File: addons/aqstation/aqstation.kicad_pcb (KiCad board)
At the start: 2 copper layers, 76 x 50 mm, 15 parts, among them J1 PMSA003, J2 Conn_02x06_Odd_Even, J3 Adafruit_I2C_Header, J5 RGB_Header, J6 Pimoroni_I2CGarden_Header, J7 StemmaQT_Qwiic_Header, J8 BME680_Header

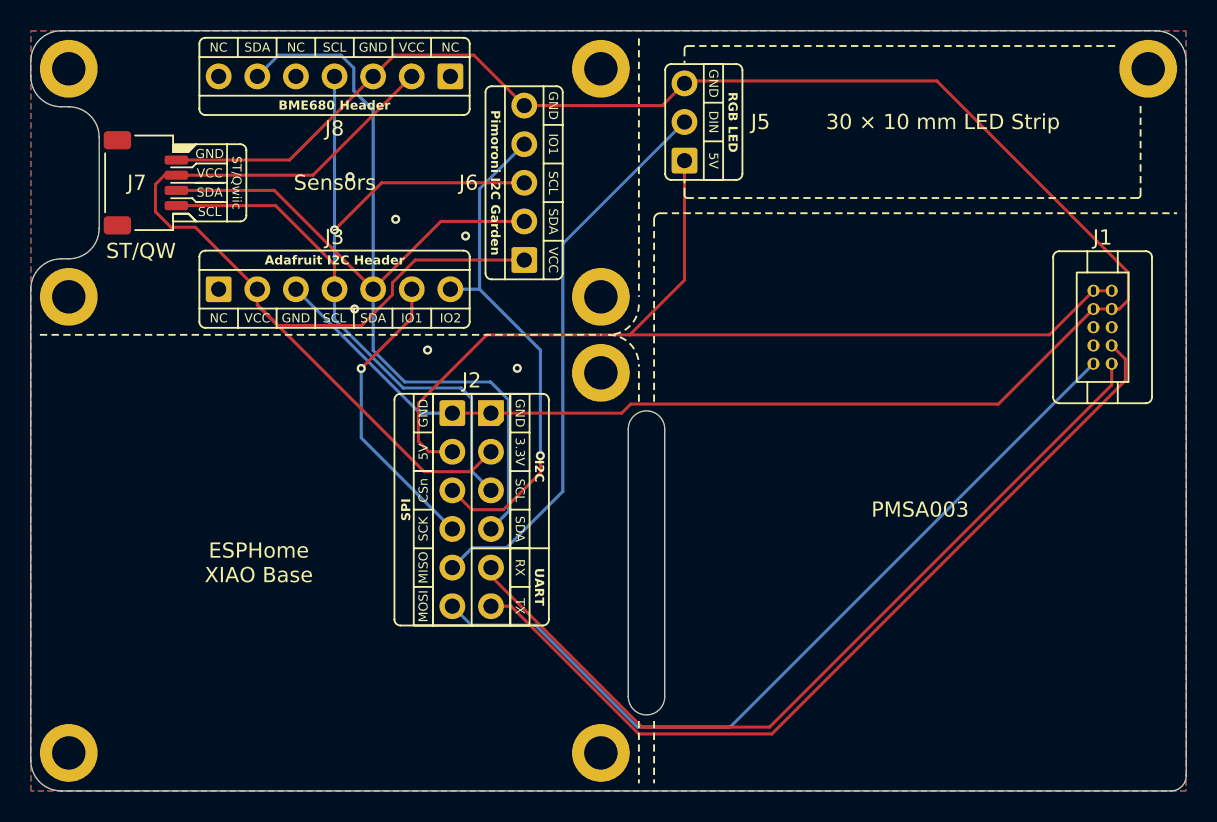
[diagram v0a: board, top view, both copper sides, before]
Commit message: More compact version of the AQStation
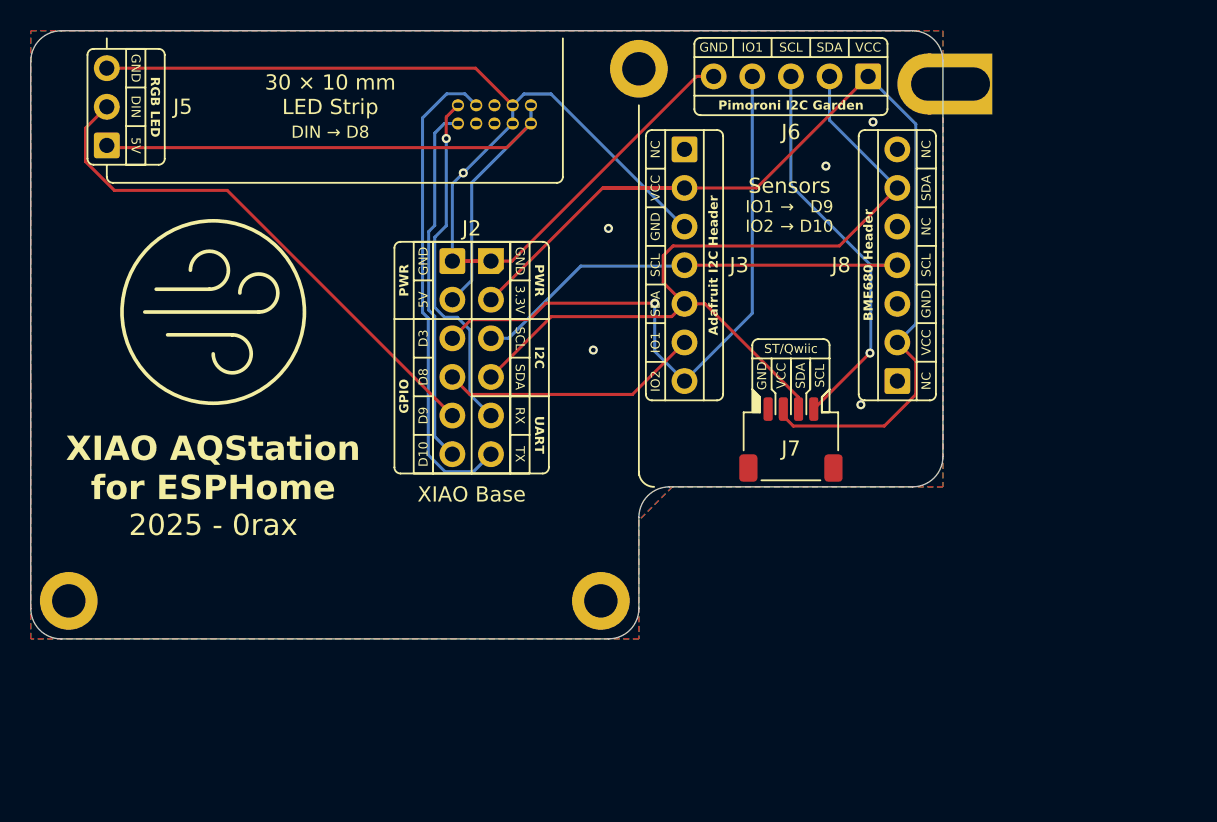
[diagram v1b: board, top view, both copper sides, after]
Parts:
- removed H1, H5, H6, H8: MountingHole_2.2mm_M2_ISO14580_Pad, MountingHole:MountingHole_2.2mm_M2_ISO14580_Pad
- H2: value MountingHole_2.2mm_M2_ISO14580_Pad -> MountingHole_M2_Slot; footprint MountingHole:MountingHole_2.2mm_M2_ISO14580_Pad -> LKBD_MountingHole:MountingHole_M2_Slot
- J1: moved to B.Cu
- moved H3 79.2 mm to (32.5, 67.5)
- moved H7 58.6 mm to (70.0, 32.5)
- moved J7 45.7 mm to (80.0, 56.9), turned to 0 degrees
- moved H4 40.3 mm to (67.5, 67.5)
- moved J1 39.8 mm to (68.0, 30.0), turned to 180 degrees
- moved J8 39.0 mm to (87.0, 45.4), turned to 180 degrees
- moved J5 38.0 mm to (35.0, 35.0)
- moved H2 24.5 mm to (92.0, 33.5), turned to 180 degrees
- moved J3 23.1 mm to (73.0, 45.4), turned to 0 degrees
- moved J6 18.9 mm to (80.0, 33.0), turned to -90 degrees
- moved J2 10.0 mm to (59.0, 51.5)
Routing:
- net GND: track 135.8 -> 79.6 mm
- net /RX: track 56.2 -> 23.1 mm, vias 0 -> 1
- net /D3: track 55.4 -> 23.7 mm
- net /TX: track 57.5 -> 31.9 mm
- net +5V: track 66.6 -> 43.6 mm
- net /SDA: track 73.7 -> 55.7 mm
- net /D10: track 33.7 -> 42.1 mm
- net /SCL: track 61.2 -> 56.1 mm
- net +3.3V: track 74.6 -> 71.7 mm
- net /D9: track 19.8 -> 17.2 mm, vias 1 -> 0
- net /D8: track 37.0 -> 35.2 mm
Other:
- board size 76 x 50 mm -> 60 x 40 mm
- board text added: "0.1600 mm / 0.1600 mm"
- board text added: "0.3000 mm"
- board text added: "1.6000 mm"
- board text added: "2"
- board text added: "60.0000 mm x 40.0000 mm"
- board text added: "BOARD CHARACTERISTICS"
- board text added: "Board Thickness:"
- board text added: "Board overall dimensions:"
- board text added: "Castellated pads:"
- board text added: "Copper Finish:"
- board text added: "Copper Layer Count:"
- board text added: "D9 D10"
- board text added: "DIN → D8"
- board text added: "Edge card connectors:"
- board text added: "HAL lead-free"
- board text added: "IO1 IO2"
- board text added: "Impedance Control:"
- board text added: "Min hole diameter:"
- board text added: "Min track/spacing:"
- board text added: "No"
- board text added: "Plated Board Edge:"
- board text added: "XIAO Base"
- board text added: "→ →"
- board text removed: "ESPHome XIAO Base"
- board text removed: "ST/QW"

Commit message: Switch LED header to just some pads
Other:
- board text added: "SET → D3"

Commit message: Remove solderpaste from pcbdraw export
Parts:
- added H5: MountingHole_2.2mm_M2_ISO14580_Pad, MountingHole:MountingHole_2.2mm_M2_ISO14580_Pad, F.Cu at (87.5, 57.5)
- renumbered H7 to H1
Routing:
- net +3.3V: track 71.7 -> 68.5 mm
- net GND: vias 6 -> 4

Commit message: Cleanup wiring
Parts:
- added H5: MountingHole_2.2mm_M2_ISO14580_Pad, MountingHole:MountingHole_2.2mm_M2_ISO14580_Pad, F.Cu at (67.5, 42.5)
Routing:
- net +3.3V: track 68.5 -> 62.0 mm
- net /D10: track 42.1 -> 39.4 mm
- net GND: track 79.6 -> 77.1 mm, vias 4 -> 3
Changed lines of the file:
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@@
 		)
 	)
+	(footprint "MountingHole:MountingHole_2.2mm_M2_ISO14580_Pad"
+		(layer "F.Cu")
+		(at 67.5 42.5)
+		(descr "Mounting Hole 2.2mm, M2, ISO14580")
+		(tags "mounting hole 2.2mm m2 iso14580")
+		(property "Reference" "H5"
+			(at 0 -2.9 0)
+			(layer "F.SilkS")
+			(hide yes)
+			(effects
+				(font
+					(size 1 1)
+					(thickness 0.15)
+				)
+			)
+		)
+		(property "Value" "MountingHole_2.2mm_M2_ISO14580_Pad"
+			(at 0 2.9 0)
+			(layer "F.Fab")
+			(effects
+				(font
+					(size 1 1)
+					(thickness 0.15)
+				)
+			)
+		)
+		(property "Datasheet" ""
+			(at 0 0 0)
+			(unlocked yes)
+			(layer "F.Fab")
+			(hide yes)
+			(effects
+				(font
+					(size 1.27 1.27)
+					(thickness 0.15)
+				)
+			)
+		)
+		(property "Description" ""
+			(at 0 0 0)
+			(unlocked yes)
+			(layer "F.Fab")
+			(hide yes)
+			(effects
+				(font
+					(size 1.27 1.27)
+					(thickness 0.15)
+				)
+			)
+		)
+		(attr board_only exclude_from_pos_files exclude_from_bom)
+		(fp_circle
+			(center 0 0)
+			(end 1.9 0)
+			(stroke
+				(width 0.15)
+				(type solid)
+			)
+			(fill no)
+			(layer "Cmts.User")
+		)
+		(fp_circle
+			(center 0 0)
+			(end 2.15 0)
+			(stroke
+				(width 0.05)
+				(type solid)
+			)
+			(fill no)
+			(layer "F.CrtYd")
+		)
+		(fp_text user "${REFERENCE}"
+			(at 0 0 0)
+			(layer "F.Fab")
+			(effects
+				(font
+					(size 1 1)
+					(thickness 0.15)
+				)
+			)
+		)
+		(pad "1" thru_hole circle
+			(at 0 0)
+			(size 3.8 3.8)
+			(drill 2.2)
+			(layers "*.Cu" "*.Mask")
+			(remove_unused_layers no)
+		)
+		(embedded_fonts no)
+	)
 	(footprint "LKBD_MountingHole:MountingHole_M2_Slot"
 		(layer "F.Cu")
@@
 	)
 	(segment
-		(start 35 32.46)
-		(end 59.26 32.46)
+		(start 60.27 45.15)
+		(end 69.52 35.9)
 		(width 0.2)
 		(layer "F.Cu")
@@
 	)
 	(segment
-		(start 57.73 45.15)
-		(end 60.27 45.15)
+		(start 35 32.46)
+		(end 59.26 32.46)
 		(width 0.2)
 		(layer "F.Cu")
@@
 	(segment
 		(start 57.73 45.15)
-		(end 61.65 45.15)
+		(end 60.27 45.15)
 		(width 0.2)
 		(layer "F.Cu")
@@
 	)
 	(segment
-		(start 61.65 45.15)
-		(end 73.8 33)
+		(start 69.52 35.9)
+		(end 72.02 35.9)
 		(width 0.2)
 		(layer "F.Cu")
@@
 	)
 	(segment
-		(start 73.8 33)
-		(end 74.92 33)
+		(start 74.92 33)
+		(end 72.02 35.9)
 		(width 0.2)
 		(layer "F.Cu")
@@
 	)
 	(via
-		(at 68 43)
+		(at 68.9 47.3)
 		(size 0.6)
 		(drill 0.3)
 		(layers "F.Cu" "B.Cu")
+		(free yes)
 		(net 1)
 	)
@@
 	)
 	(via
-		(at 67 51)
-		(size 0.6)
-		(drill 0.3)
-		(layers "F.Cu" "B.Cu")
-		(net 1)
-	)
-	(via
 		(at 82.3 38.9)
 		(size 0.6)
@@
 	)
 	(segment
-		(start 73 40.34)
-		(end 71.64 40.34)
+		(start 60.56 47.4)
+		(end 60.27 47.69)
 		(width 0.2)
 		(layer "F.Cu")
@@
 	)
 	(segment
-		(start 79.5 55.659999)
-		(end 79.940001 56.1)
+		(start 77.74 40.34)
+		(end 85.08 33)
 		(width 0.2)
 		(layer "F.Cu")
@@
 	)
 	(segment
-		(start 87 51.009196)
-		(end 87 50.5)
+		(start 73 40.34)
+		(end 73 40.7)
 		(width 0.2)
 		(layer "F.Cu")
@@
 	)
 	(segment
-		(start 67.62 40.34)
-		(end 77.74 40.34)
+		(start 66.3 47.4)
+		(end 60.56 47.4)
+		(width 0.2)
+		(layer "F.Cu")
+		(net 2)
+	)
+	(segment
+		(start 79.5 55.659999)
+		(end 79.940001 56.1)
 		(width 0.2)
 		(layer "F.Cu")
@@
 	)
 	(segment
-		(start 67.62 40.34)
-		(end 73 40.34)
+		(start 87 51.009196)
+		(end 87 50.5)
 		(width 0.2)
 		(layer "F.Cu")
@@
 	)
 	(segment
-		(start 60.27 47.69)
-		(end 67.62 40.34)
+		(start 73 40.7)
+		(end 66.3 47.4)
 		(width 0.2)
 		(layer "F.Cu")
@@
 	)
 	(segment
-		(start 77.74 40.34)
-		(end 85.08 33)
+		(start 73 40.34)
+		(end 77.74 40.34)
 		(width 0.2)
 		(layer "F.Cu")
@@
 	)
 	(segment
-		(start 87 40.34)
-		(end 83.19 44.15)
+		(start 63.14 49.9)
+		(end 60.27 52.77)
 		(width 0.2)
 		(layer "F.Cu")
@@
 	)
 	(segment
-		(start 72.16 48.8)
-		(end 64.24 48.8)
+		(start 87 40.34)
+		(end 83.19 44.15)
 		(width 0.2)
 		(layer "F.Cu")
@@
 	)
 	(segment
-		(start 64.24 48.8)
-		(end 60.27 52.77)
-		(width 0.2)
-		(layer "F.Cu")
-		(net 4)
-	)
-	(segment
 		(start 83.19 44.15)
 		(end 72.25 44.15)
@@
 	(segment
 		(start 73 47.96)
-		(end 72.16 48.8)
+		(end 71.06 49.9)
 		(width 0.2)
 		(layer "F.Cu")
@@
 	)
 	(segment
+		(start 71.06 49.9)
+		(end 63.14 49.9)
+		(width 0.2)
+		(layer "F.Cu")
+		(net 4)
+	)
+	(segment
 		(start 71.6 46.56)
 		(end 73 47.96)
@@
 	)
 	(segment
-		(start 69.579 53.921)
-		(end 73 50.5)
+		(start 58.96 54)
+		(end 61.2 54)
 		(width 0.2)
 		(layer "F.Cu")
@@
 	)
 	(segment
-		(start 58.881 53.921)
-		(end 69.579 53.921)
+		(start 61.2 54)
+		(end 64.7 50.5)
 		(width 0.2)
 		(layer "F.Cu")
@@
 	)
 	(segment
-		(start 57.73 52.77)
-		(end 58.881 53.921)
+		(start 64.7 50.5)
+		(end 73 50.5)
 		(width 0.2)
 		(layer "F.Cu")
@@
 	)
 	(segment
-		(start 58.96 49)
-		(end 62.8 49)
-		(width 0.2)
-		(layer "F.Cu")
-		(net 18)
-	)
-	(segment
-		(start 62.8 49)
-		(end 63.8818 47.9182)
+		(start 57.73 52.77)
+		(end 58.96 54)
 		(width 0.2)
 		(layer "F.Cu")
-		(net 18)
+		(net 17)
 	)
 	(segment
-		(start 57.73 50.23)
+		(start 69.1 49)
 		(end 58.96 49)
 		(width 0.2)
@@
 	)
 	(segment
-		(start 63.8818 47.9182)
-		(end 71.0427 47.9182)
+		(start 58.96 49)
+		(end 57.73 50.23)
 		(width 0.2)
 		(layer "F.Cu")
@@
 	)
 	(via
-		(at 71.0427 47.9182)
+		(at 69.1 49)
 		(size 0.6)
 		(drill 0.3)
@@
 	)
 	(segment
+		(start 73 52.9182)
+		(end 73 53.04)
+		(width 0.2)
+		(layer "B.Cu")
+		(net 18)
+	)
+	(segment
 		(start 77.46 48.58)
 		(end 73 53.04)
@@
 	)
 	(segment
-		(start 71.0427 51.0827)
-		(end 71.0427 47.9182)
+		(start 69.1 49)
+		(end 69.1 49.0182)
 		(width 0.2)
 		(layer "B.Cu")
@@
 	)
 	(segment
-		(start 73 53.04)
-		(end 71.0427 51.0827)
+		(start 69.1 49.0182)
+		(end 73 52.9182)
 		(width 0.2)
 		(layer "B.Cu")

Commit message: Finalize aqstation
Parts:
- renumbered J2 to J1, J1 to J2, J6 to J4, J8 to J5, J7 to J6, J5 to J7
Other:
- board text added: "J4"
- board text added: "J5"
- board text removed: "J7"
- board text removed: "J8"

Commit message: Fix issues with the initial version and add support for DFRobot BME breakouts
Update documentation
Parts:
- removed H2: MountingHole_M2_Slot, LKBD_MountingHole:MountingHole_M2_Slot
- J3: value Adafruit_I2C_Header -> DFRobot_BME680_Header; footprint Header:Adafruit_I2C_Header -> Header:DFRobot_BME680_Header
- J4: value Pimoroni_I2CGarden_Header -> Adafruit_I2C_Header; footprint Header:Pimoroni_I2CGarden_Header -> Header:Adafruit_I2C_Header
- J5: value BME680_Header -> Adafruit_BME680_Header; footprint Header:BME680_Header -> Header:Adafruit_BME680_Header
- moved J3 14.8 mm to (81.0, 33.0), turned to -90 degrees
- moved J4 14.3 mm to (73.0, 45.4), turned to 0 degrees
- renumbered H5 to H6
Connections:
- net /D3 renamed /SET
- net /D8 renamed /LEDIO
- J1 pad 6: /D10 -> /EN
- J1 pad 8: /D9 -> /ADDR
- J3 pad 1: unconnected-(J3-5V-Pad1) -> +3.3V
- J3 pad 2: +3.3V -> GND
- J3 pad 3: GND -> /SDA
- J3 pad 4: /SCL -> /EN
- J3 pad 5: /SDA -> /SCL
- J3 pad 6: /D9 -> /ADDR
- J4 pad 1: +3.3V -> unconnected-(J4-5V-Pad1)
- J4 pad 2: /SDA -> +3.3V
- J4 pad 3: /SCL -> GND
- J4 pad 4: /D10 -> /SCL
- J4 pad 5: GND -> /SDA
- J5 pad 5: unconnected-(J5-SDO-Pad5) -> /ADDR
- J5 pad 7: unconnected-(J5-CS-Pad7) -> /EN
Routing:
- net /EN: track 0.00 -> 54.1 mm, vias 0 -> 1
- net /ADDR: track 0.00 -> 53.3 mm
- net /D10: track 39.4 -> 0.00 mm, vias 1 -> 0
- net GND: track 77.1 -> 42.1 mm, vias 3 -> 5
- net /D9: track 17.2 -> 0.00 mm
- net /SCL: track 56.3 -> 50.2 mm, vias 1 -> 0
- net /SDA: track 55.7 -> 51.1 mm
- net +3.3V: track 62.0 -> 64.2 mm
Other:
- board text added: "Adafruit BME280 & BME68X breakouts"
- board text added: "D8 D3"
- board text added: "DFRobot BME680 & BME688 (Fermion)"
- board text added: "DIN → D9"
- board text added: "PMSA003"
- board text added: "Sensor"
- board text removed: "Adafruit BME28X/68X DFRobot Fermion BME680"
- board text removed: "D9 D10"
- board text removed: "DIN → D8"
- board text removed: "Pimoroni I2C breakouts (Breakout Garden)"
- board text removed: "Sensors"
- board text removed: "XIAO Base"
